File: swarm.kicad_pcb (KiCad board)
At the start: 2 copper layers, 60 x 30 mm, 24 parts, among them P1 USB_OTG, P2 CONN_01X05, P3 CONN_02X20, SW1 SW_PUSH, U1 LM3671MF-3.3, U2 STM32F103RETx, Y1 Crystal

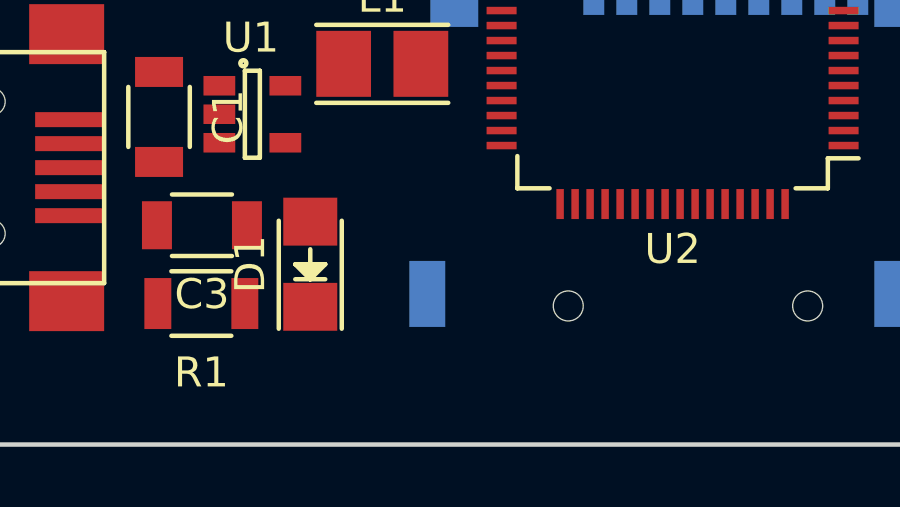
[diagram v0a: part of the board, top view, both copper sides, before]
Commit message: Adds U3 (APA102 LED) to pcbnew
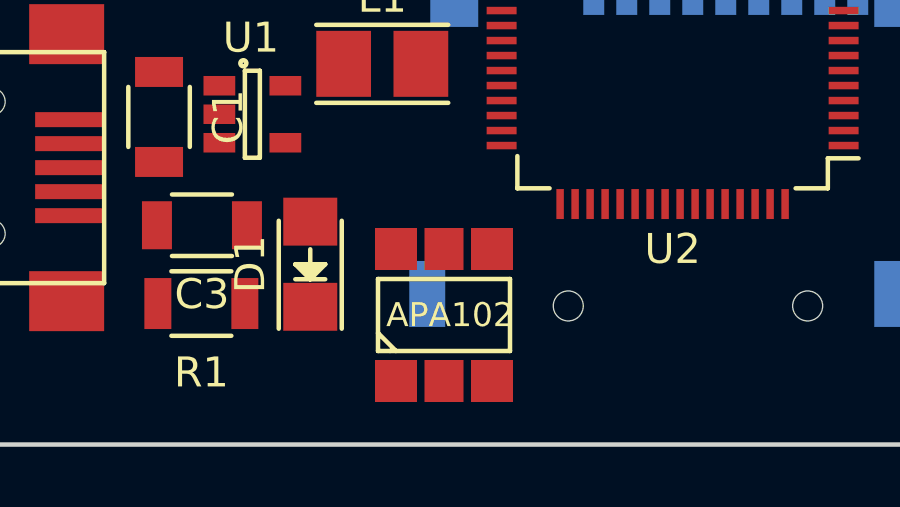
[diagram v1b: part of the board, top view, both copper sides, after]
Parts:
- added U3: APA102, volium:APA102, F.Cu at (120.8, 95.7)
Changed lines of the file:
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@@
     (tracks 0)
     (zones 0)
-    (modules 24)
-    (nets 87)
+    (modules 25)
+    (nets 93)
   )
   (page A4)
@@
   (net 85 "Net-(U2-Pad50)")
   (net 86 "Net-(U2-Pad60)")
+  (net 87 "Net-(U3-Pad3)")
+  (net 88 "Net-(U3-Pad4)")
+  (net 89 "Net-(U3-Pad5)")
+  (net 90 "Net-(U3-Pad2)")
+  (net 91 "Net-(U3-Pad1)")
+  (net 92 "Net-(U3-Pad6)")
   (net_class Default "This is the default net class."
     (clearance 0.1524)
@@
     (add_net "Net-(U2-Pad8)")
     (add_net "Net-(U2-Pad9)")
+    (add_net "Net-(U3-Pad1)")
+    (add_net "Net-(U3-Pad2)")
+    (add_net "Net-(U3-Pad3)")
+    (add_net "Net-(U3-Pad4)")
+    (add_net "Net-(U3-Pad5)")
+    (add_net "Net-(U3-Pad6)")
     (add_net VCC)
   )
@@
     )
   )
+  (module volium:APA102 (layer Top)
+    (at 120.828 95.682)
+    (fp_text reference U3 (at 0.2 -4) (layer F.SilkS) hide
+      (effects (font (size 1.5 1.5) (thickness 0.15)))
+    )
+    (fp_text value APA102 (at 0.2 0) (layer F.SilkS)
+      (effects (font (size 0.8 0.8) (thickness 0.15)))
+    )
+    (fp_line (start -2.2 0.6) (end -1.6 1.2) (layer F.SilkS) (width 0.15))
+    (fp_line (start 2.2 1.2) (end -1.8 1.2) (layer F.SilkS) (width 0.15))
+    (fp_line (start -2.2 -1.2) (end 2.2 -1.2) (layer F.SilkS) (width 0.15))
+    (fp_line (start -1.8 1.2) (end -2.2 1.2) (layer F.SilkS) (width 0.15))
+    (fp_line (start 2.2 -1.2) (end 2.2 1.2) (layer F.SilkS) (width 0.15))
+    (fp_line (start -2.2 -1.2) (end -2.2 1.2) (layer F.SilkS) (width 0.15))
+    (pad 3 smd rect (at 1.6 2.2 90) (size 1.4 1.4) (layers Top F.Paste F.Mask)
+      (net 87 "Net-(U3-Pad3)"))
+    (pad 4 smd rect (at 1.6 -2.2 90) (size 1.4 1.4) (layers Top F.Paste F.Mask)
+      (net 88 "Net-(U3-Pad4)"))
+    (pad 5 smd rect (at 0 -2.2 90) (size 1.4 1.3) (layers Top F.Paste F.Mask)
+      (net 89 "Net-(U3-Pad5)"))
+    (pad 2 smd rect (at 0 2.2 90) (size 1.4 1.3) (layers Top F.Paste F.Mask)
+      (net 90 "Net-(U3-Pad2)"))
+    (pad 1 smd rect (at -1.6 2.2 90) (size 1.4 1.4) (layers Top F.Paste F.Mask)
+      (net 91 "Net-(U3-Pad1)"))
+    (pad 6 smd rect (at -1.6 -2.2 90) (size 1.4 1.4) (layers Top F.Paste F.Mask)
+      (net 92 "Net-(U3-Pad6)"))
+    (model C:/Users/rotorres/Downloads/APA102C.wrl
+      (at (xyz 0 0 0))
+      (scale (xyz 0.393701 0.393701 0.393701))
+      (rotate (xyz 0 0 -90))
+    )
+  )

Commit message: Moves some components around, no significant changes
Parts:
- C13, C4, C6, C7: moved to B.Cu
- moved U3 41.3 mm to (162.2, 95.9), turned to 90 degrees
- moved C9 24.6 mm to (129.8, 79.7), turned to 0 degrees
- moved C12 22.7 mm to (130.3, 94.8), turned to 180 degrees
- moved C13 21.7 mm to (134.3, 89.8)
- moved C8 20.8 mm to (123.2, 77.5), turned to 0 degrees
- moved R1 17.5 mm to (103.0, 80.8), turned to 90 degrees
- moved C10 15.7 mm to (123.3, 79.7), turned to 0 degrees
- moved D1 15.4 mm to (104.3, 84.4), turned to 0 degrees
- moved C3 13.9 mm to (105.6, 80.8), turned to 90 degrees
- moved C11 13.5 mm to (119.4, 91.0)
- moved C1 11.2 mm to (109.4, 78.0), turned to 180 degrees
- moved C4 10.8 mm to (130.3, 89.5), turned to 270 degrees
- moved L1 9.94 mm to (109.2, 84.5), turned to 180 degrees
- moved Y1 9.92 mm to (135.0, 88.6)
- moved U1 9.44 mm to (109.2, 81.1), turned to 270 degrees
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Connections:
- U2 pad 21: Net-(U2-Pad21) -> /RGB_LED_CIN
- U2 pad 23: Net-(U2-Pad23) -> /RGB_LED_DIN
- U3 pad 1: Net-(U3-Pad1) -> /RGB_LED_DIN
- U3 pad 2: Net-(U3-Pad2) -> /RGB_LED_CIN
- U3 pad 3: Net-(U3-Pad3) -> GND
- U3 pad 4: Net-(U3-Pad4) -> VCC

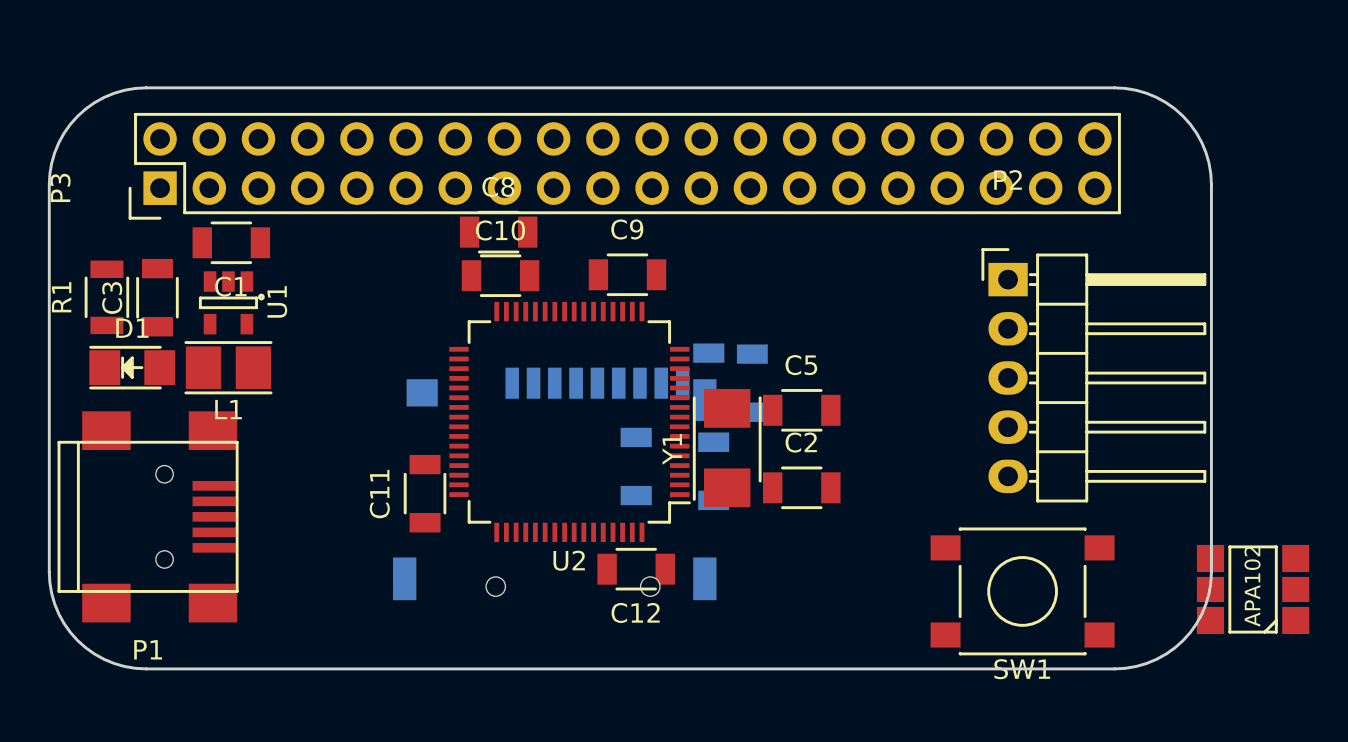
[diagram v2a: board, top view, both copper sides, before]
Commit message: Moving towards routing Switched to 0805 components Locked connectors and MCU, routed part of LCD_DBXX signals
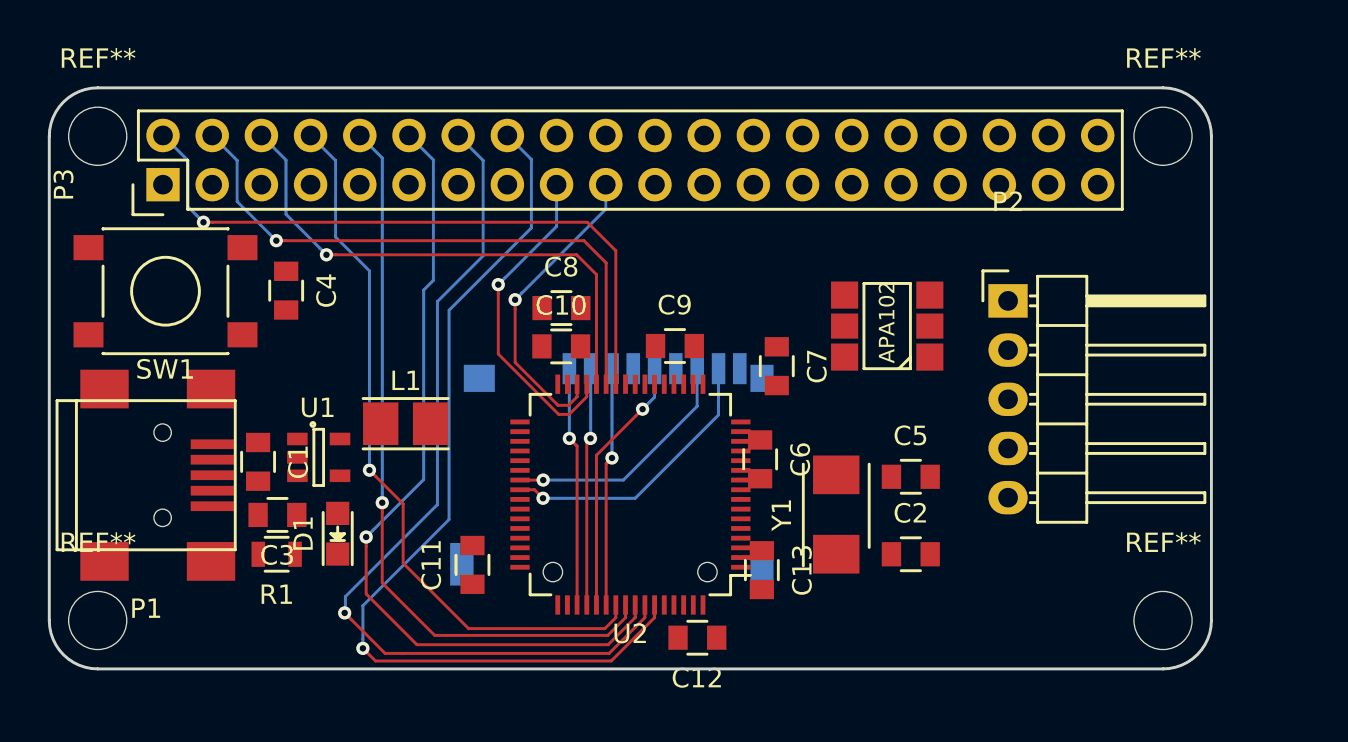
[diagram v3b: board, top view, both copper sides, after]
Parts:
- added REF**: MountingHole_3mm, Mounting_Holes:MountingHole_3mm, F.Cu at (102.5, 97.5)
- added REF**: MountingHole_3mm, Mounting_Holes:MountingHole_3mm, F.Cu at (157.5, 97.5)
- added REF**: MountingHole_3mm, Mounting_Holes:MountingHole_3mm, F.Cu at (157.5, 72.5)
- added REF**: MountingHole_3mm, Mounting_Holes:MountingHole_3mm, F.Cu at (102.5, 72.5)
- C1, C10, C11, C12, C2, C3, C5, C8, C9: footprint Capacitors_SMD:C_1206 -> Capacitors_SMD:C_0805
- C13, C4, C6, C7: footprint Capacitors_SMD:C_1206 -> Capacitors_SMD:C_0805; moved to F.Cu
- D1: footprint LEDs:LED_1206 -> LEDs:LED_0805
- R1: footprint Resistors_SMD:R_1206 -> Resistors_SMD:R_0805
- moved SW1 46.9 mm to (106.0, 80.5)
- moved U3 23.3 mm to (143.3, 82.3)
- moved C4 20.2 mm to (112.2, 80.5)
- moved R1 15.9 mm to (111.7, 94.1), turned to 180 degrees
- moved D1 13.6 mm to (114.9, 93.0), turned to 90 degrees
- moved C3 12.8 mm to (111.8, 92.0), turned to 180 degrees
- moved C1 11.4 mm to (110.8, 89.3), turned to 270 degrees
- moved L1 9.60 mm to (118.4, 87.3), turned to 0 degrees
- moved U1 9.24 mm to (113.9, 89.1), turned to 0 degrees
- moved Y1 6.59 mm to (140.6, 92.0)
- moved C2 6.59 mm to (144.5, 94.1)
- moved C5 6.59 mm to (144.5, 90.1)
- moved C13 5.68 mm to (136.8, 94.9), turned to 270 degrees
- moved C8 5.09 mm to (126.4, 81.4)
- moved U2 4.90 mm to (130.0, 91.0)
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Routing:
- net /LCD_D7: track 0.00 -> 47.5 mm, vias 0 -> 1
- net /LCD_D6: track 0.00 -> 45.9 mm, vias 0 -> 1
- net /LCD_D5: track 0.00 -> 41.8 mm, vias 0 -> 1
- net /LCD_D4: track 0.00 -> 38.3 mm, vias 0 -> 1
- net /LCD_D3: track 0.00 -> 37.3 mm, vias 0 -> 1
- net /LCD_D0: track 0.00 -> 34.1 mm, vias 0 -> 1
- net /LCD_D1: track 0.00 -> 30.6 mm, vias 0 -> 1
- net /LCD_D2: track 0.00 -> 27.6 mm, vias 0 -> 1
- net /LCD_D10: track 0.00 -> 16.9 mm, vias 0 -> 1
- net /LCD_D11: track 0.00 -> 16.1 mm, vias 0 -> 1
- net /SDIO_D1: track 0.00 -> 14.6 mm, vias 0 -> 1
- net /SDIO_CLK: track 0.00 -> 13.4 mm, vias 0 -> 1
- net /SDIO_D0: track 0.00 -> 12.7 mm, vias 0 -> 1
- net /SDIO_D2: track 0.00 -> 12.4 mm, vias 0 -> 1
- net /SDIO_CMD: track 0.00 -> 12.3 mm, vias 0 -> 1
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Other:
- outline, holes or cut-outs redrawn

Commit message: Fixes issue with GND and Vdd swapped for micro SD connector
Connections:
- XS1 pad 4: GND -> +3V3
- XS1 pad 6: +3V3 -> GND
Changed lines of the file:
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@@
   (general
     (links 92)
-    (no_connects 81)
+    (no_connects 76)
     (area 99.924999 69.924999 160.075001 100.075001)
     (thickness 1.6002)
@@
     (fp_line (start -7.35 10) (end -7.35 -3.3) (layer B.Fab) (width 0.05))
     (pad 6 smd rect (at 7.75 0.4 180) (size 1.2 2.2) (layers Bottom B.Paste B.Mask)
-      (net 2 +3V3))
+      (net 1 GND))
     (pad 6 smd rect (at -7.75 0.4 180) (size 1.2 2.2) (layers Bottom B.Paste B.Mask)
-      (net 2 +3V3))
+      (net 1 GND))
     (pad 6 smd rect (at 6.85 10 180) (size 1.6 1.4) (layers Bottom B.Paste B.Mask)
-      (net 2 +3V3))
+      (net 1 GND))
     (pad 6 smd rect (at -7.75 10 180) (size 1.2 1.4) (layers Bottom B.Paste B.Mask)
-      (net 2 +3V3))
+      (net 1 GND))
     (pad 9 smd rect (at -6.6 10.5 180) (size 0.7 1.6) (layers Bottom B.Paste B.Mask)
       (net 32 /SDIO_CD))
@@
       (net 20 /SDIO_D1))
     (pad 6 smd rect (at -3.3 10.5 180) (size 0.7 1.6) (layers Bottom B.Paste B.Mask)
-      (net 2 +3V3))
+      (net 1 GND))
     (pad 5 smd rect (at -2.2 10.5 180) (size 0.7 1.6) (layers Bottom B.Paste B.Mask)
       (net 23 /SDIO_CLK))
     (pad 4 smd rect (at -1.1 10.5 180) (size 0.7 1.6) (layers Bottom B.Paste B.Mask)
-      (net 1 GND))
+      (net 2 +3V3))
     (pad 1 smd rect (at 2.2 10.5 180) (size 0.7 1.6) (layers Bottom B.Paste B.Mask)
       (net 21 /SDIO_D2))

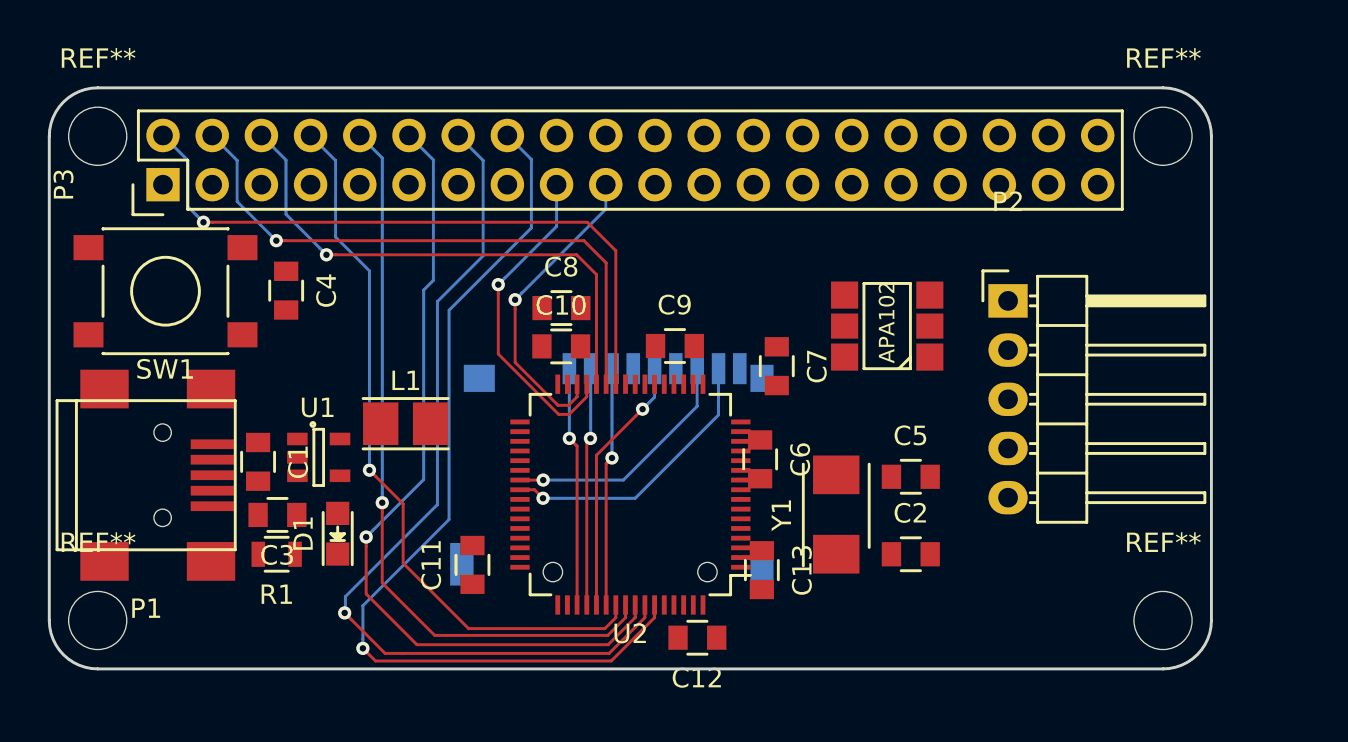
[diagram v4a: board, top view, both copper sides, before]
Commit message: Routed all LCD-related signals
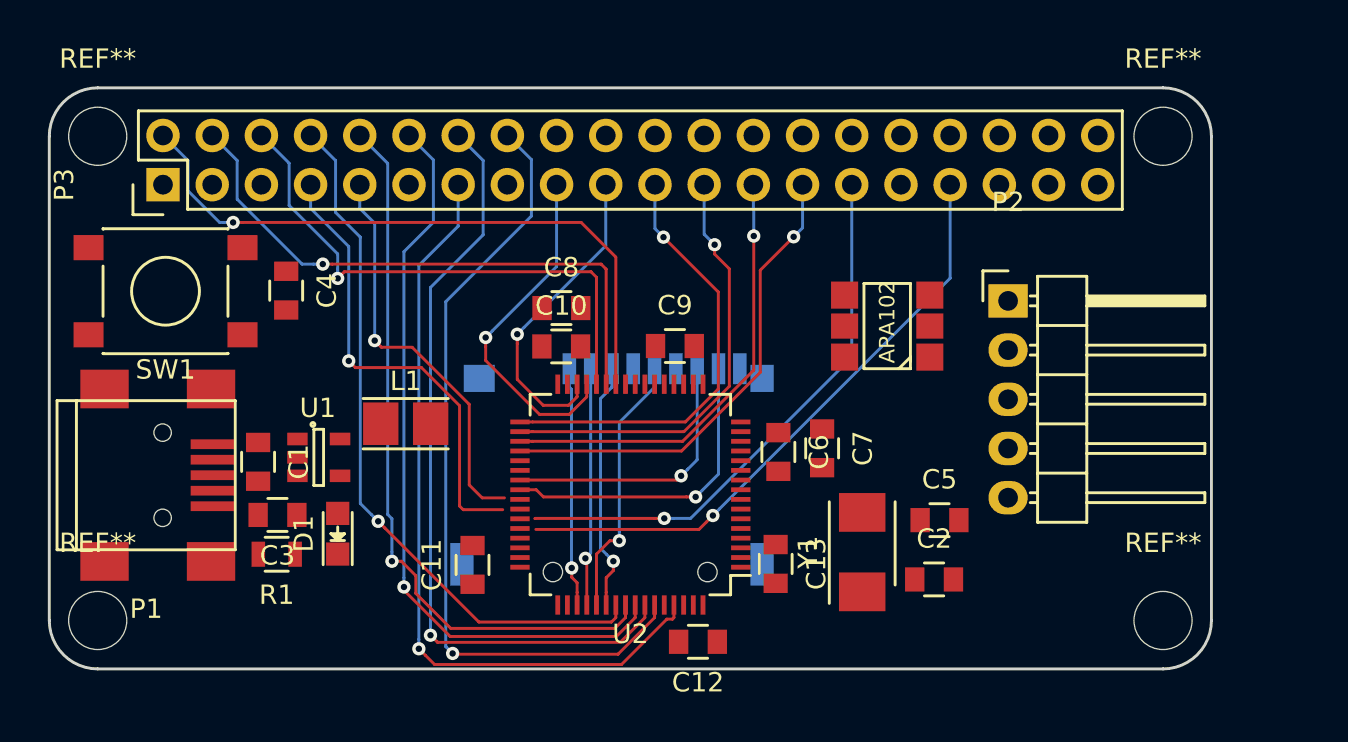
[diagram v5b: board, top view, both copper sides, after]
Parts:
- moved C7 4.84 mm to (139.9, 88.6)
- moved C5 2.68 mm to (146.0, 92.3)
- moved Y1 2.36 mm to (142.0, 94.0)
- moved C2 1.77 mm to (145.7, 95.4)
- moved C6 1.01 mm to (137.6, 88.8)
- moved C13 0.78 mm to (137.5, 94.6)
- moved C12 0.21 mm to (133.5, 98.6)
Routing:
- net /LCD_D8: track 0.00 -> 40.0 mm, vias 0 -> 1
- net /LCD_RST: track 0.00 -> 31.6 mm, vias 0 -> 1
- net /LCD_CS: track 0.00 -> 28.7 mm, vias 0 -> 1
- net /LCD_D15: track 0.00 -> 24.7 mm, vias 0 -> 1
- net /LCD_RS: track 0.00 -> 24.1 mm, vias 0 -> 1
- net /LCD_D14: track 0.00 -> 23.2 mm, vias 0 -> 1
- net /LCD_D12: track 0.00 -> 22.8 mm, vias 0 -> 1
- net /LCD_D13: track 0.00 -> 22.7 mm, vias 0 -> 1
- net /LCD_WR: track 0.00 -> 20.9 mm, vias 0 -> 1
- net /LCD_D7: track 47.5 -> 41.1 mm
- net /LCD_D6: track 45.9 -> 39.9 mm
- net /LCD_D5: track 41.8 -> 38.6 mm
- net /SDIO_D1: track 14.6 -> 16.3 mm
- net /SDIO_D0: track 12.7 -> 14.3 mm
- net /LCD_D10: track 16.9 -> 18.0 mm
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
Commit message: Connected USB (D+, D-) signals (routable)
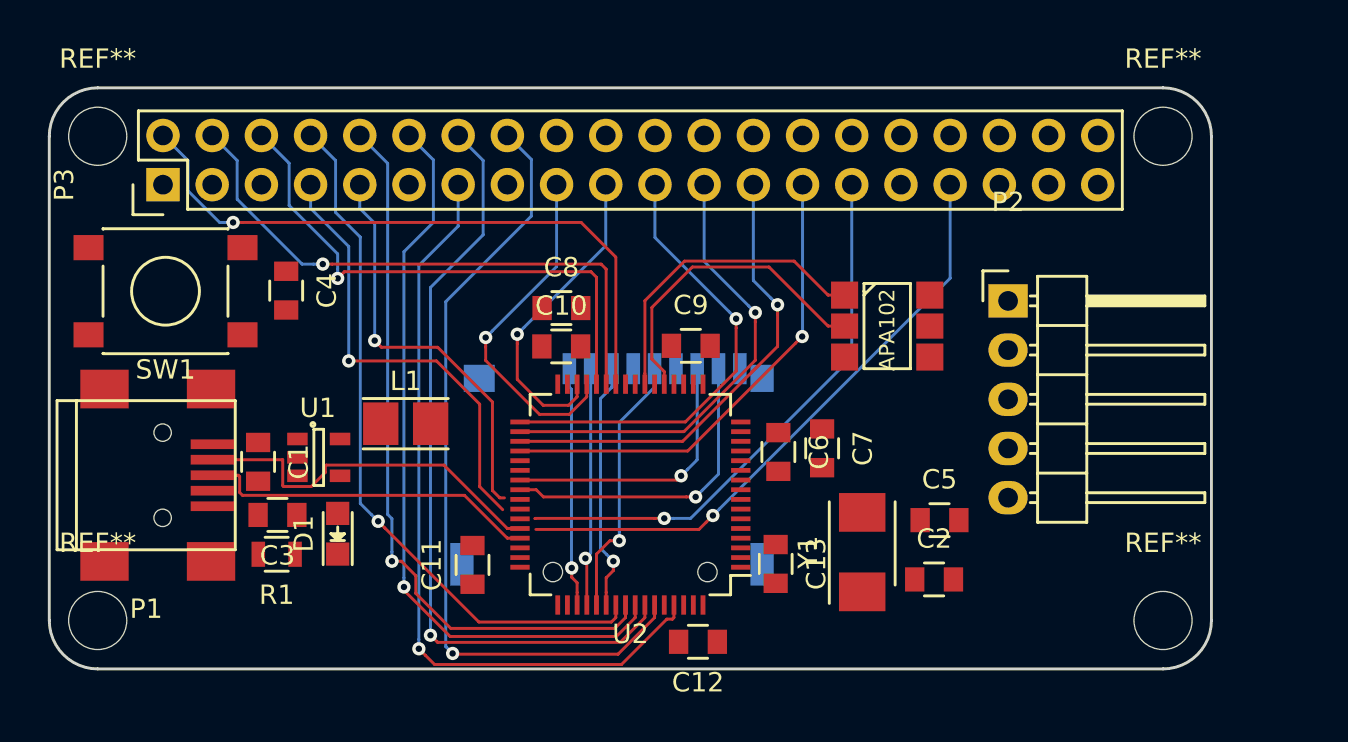
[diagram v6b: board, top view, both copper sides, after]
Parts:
- moved C9 0.82 mm to (133.1, 83.3)
- turned U3 to 270 degrees
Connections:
- P1 pad 2: Net-(P1-Pad2) -> /USB_D-
- P1 pad 3: Net-(P1-Pad3) -> /USB_D+
- U2 pad 44: Net-(U2-Pad44) -> /USB_D-
- U2 pad 45: Net-(U2-Pad45) -> /USB_D+
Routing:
- net /USB_D-: track 0.00 -> 19.2 mm
- net /USB_D+: track 0.00 -> 17.7 mm
- net /RGB_LED_CIN: track 0.00 -> 16.3 mm
- net /RGB_LED_DIN: track 0.00 -> 16.2 mm
- net /LCD_D13: track 22.7 -> 23.8 mm
- net /LCD_D14: track 23.2 -> 24.2 mm
- net /LCD_D12: track 22.8 -> 23.6 mm
- net /LCD_RS: track 24.1 -> 23.5 mm
